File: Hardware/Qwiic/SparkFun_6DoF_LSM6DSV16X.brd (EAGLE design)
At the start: 25.4 x 25.4 mm, 78 parts, among them J1 QWIIC_RIGHT_ANGLE, J2 QWIIC_RIGHT_ANGLE, U2 LSM6DSV16X

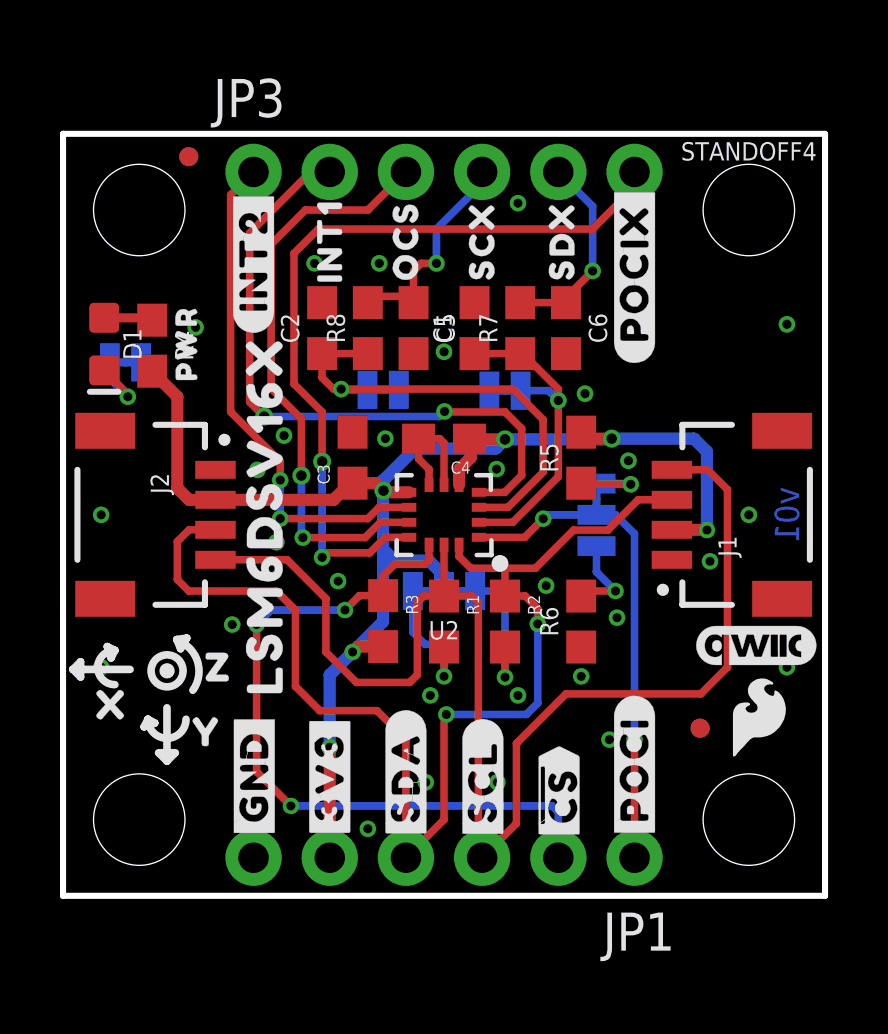
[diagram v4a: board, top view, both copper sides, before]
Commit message: Adds note about "Qvar sensing"
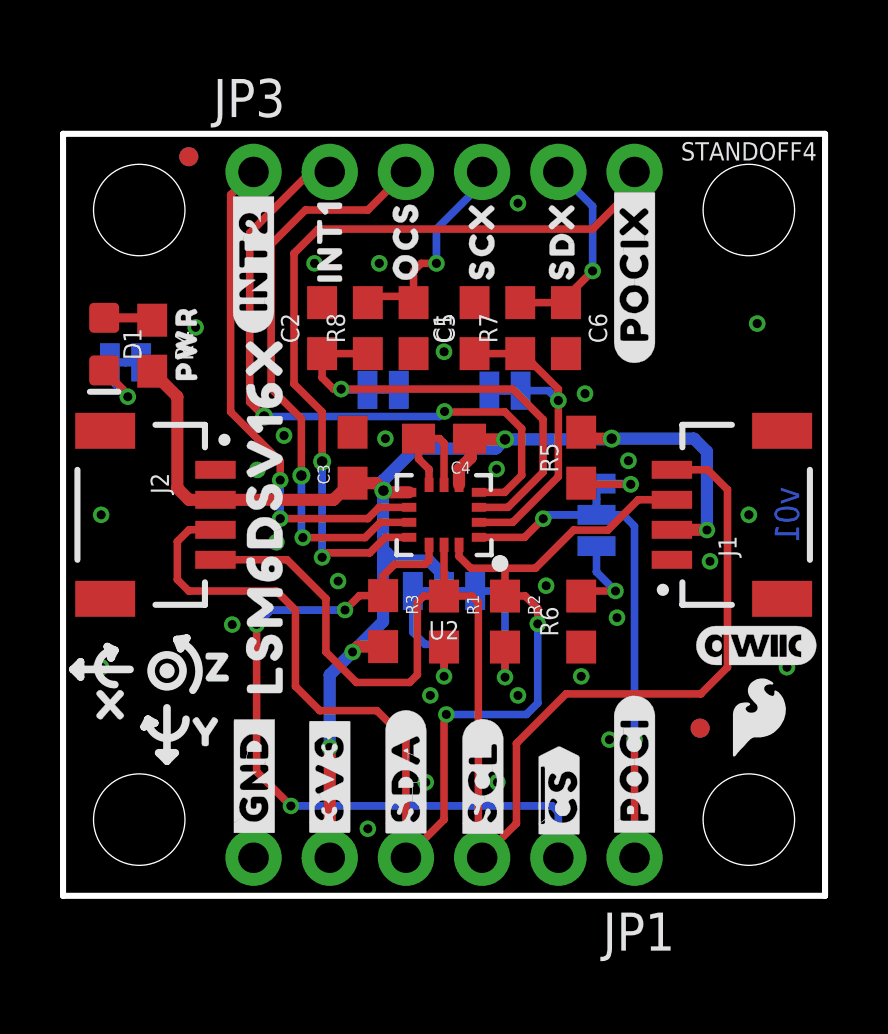
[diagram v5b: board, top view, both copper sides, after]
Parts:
- moved LOGO2 4.41 mm to (23.1, 19.1), turned to 270 degrees
- moved U$31 0.13 mm to (8.10, 12.7)
- moved U$46 0.13 mm to (6.48, 12.7)
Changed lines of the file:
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@@
 <setting verticaltext="up"/>
 </settings>
-<grid distance="0.05" unitdist="inch" unit="inch" style="dots" multiple="1" display="yes" altdistance="0.005" altunitdist="inch" altunit="inch"/>
+<grid distance="0.05" unitdist="inch" unit="inch" style="dots" multiple="1" display="yes" altdistance="0.001" altunitdist="inch" altunit="inch"/>
 <layers>
 <layer number="1" name="Top" color="4" fill="1" visible="yes" active="yes"/>
@@
 <layer number="27" name="tValues" color="7" fill="1" visible="no" active="yes"/>
 <layer number="28" name="bValues" color="7" fill="1" visible="no" active="yes"/>
-<layer number="29" name="tStop" color="7" fill="3" visible="yes" active="yes"/>
+<layer number="29" name="tStop" color="7" fill="3" visible="no" active="yes"/>
 <layer number="30" name="bStop" color="7" fill="6" visible="no" active="yes"/>
 <layer number="31" name="tCream" color="7" fill="4" visible="no" active="yes"/>
@@
 <attribute name="VALUE" x="13.716" y="16.383" size="0.4064" layer="27" font="vector" rot="R180"/>
 </element>
-<element name="LOGO2" library="SparkFun-Aesthetics" package="OSHW-LOGO-MINI" value="OSHW-LOGOMINI" x="23.7744" y="14.71295" smashed="yes" rot="MR0"/>
+<element name="LOGO2" library="SparkFun-Aesthetics" package="OSHW-LOGO-MINI" value="OSHW-LOGOMINI" x="23.13305" y="19.0754" smashed="yes" rot="MR270"/>
 <element name="STANDOFF1" library="SparkFun-Hardware" package="STAND-OFF-TIGHT" value="STAND-OFFTIGHT" x="2.54" y="22.86" smashed="yes"/>
 <element name="STANDOFF2" library="SparkFun-Hardware" package="STAND-OFF-TIGHT" value="STAND-OFFTIGHT" x="2.54" y="2.54" smashed="yes"/>
@@
 <element name="U$3" library="top" package="##CS##7" value="" x="16.5354" y="3.3528" smashed="yes" rot="R90"/>
 <element name="U$27" library="bot" package="##CS##8" value="" x="16.5354" y="3.3528" smashed="yes" rot="MR270"/>
-<element name="U$31" library="top" package="6DOF12" value="" x="7.9756" y="12.7" smashed="yes" rot="MR270"/>
+<element name="U$31" library="top" package="6DOF12" value="" x="8.1026" y="12.7" smashed="yes" rot="MR270"/>
 <element name="R5" library="SparkFun-Resistors" package="0603" value="10k" x="17.272" y="14.605" smashed="yes" rot="R90">
 <attribute name="NAME" x="16.51" y="14.605" size="0.6096" layer="25" font="vector" ratio="20" rot="R90" align="bottom-center"/>
@@
 <element name="U$42" library="top" package="#SDX#20" value="" x="14.732" y="15.367" smashed="yes" rot="MR0"/>
 <element name="U$43" library="top" package="#SCX#19" value="" x="10.668" y="15.367" smashed="yes" rot="MR0"/>
-<element name="U$46" library="top" package="LSM6DSV16X37" value="" x="6.35" y="12.7" smashed="yes" rot="MR270"/>
+<element name="U$46" library="top" package="LSM6DSV16X37" value="" x="6.477" y="12.7" smashed="yes" rot="MR270"/>
 <element name="U$47" library="top" package="LSM6DSV16X37" value="" x="6.731" y="12.7" smashed="yes" rot="R90"/>
 <element name="C5" library="SparkFun-Capacitors" package="0603" value="110pF" x="11.684" y="18.923" smashed="yes" rot="R270">
@@
 <via x="12.7" y="18.1356" extent="1-16" drill="0.3048"/>
 <via x="12.0904" y="3.7846" extent="1-16" drill="0.3"/>
-<via x="24.13" y="19.05" extent="1-16" drill="0.3048"/>
+<via x="23.1394" y="19.0754" extent="1-16" drill="0.3048"/>
 <via x="22.86" y="12.7" extent="1-16" drill="0.3048"/>
 <wire x1="12.2" y1="13.7" x2="12.2" y2="14.216" width="0.254" layer="1"/>
@@
 <wire x1="16.00481875" y1="12.57018125" x2="16.1346375" y2="12.7" width="0.254" layer="16"/>
 <wire x1="16.1346375" y1="12.7" x2="17.78" y2="12.7" width="0.254" layer="16"/>
-<wire x1="17.78" y1="12.7" x2="18.415" y2="12.7" width="0.254" layer="16"/>
+<wire x1="17.78" y1="12.7" x2="18.669" y2="12.7" width="0.254" layer="16"/>
 <via x="19.05" y="5.207" extent="1-16" drill="0.3"/>
 <contactref element="JP1" pad="1"/>
 <wire x1="19.05" y1="5.207" x2="19.05" y2="1.27" width="0.254" layer="1"/>
 <wire x1="19.0476" y1="5.2094" x2="19.05" y2="5.207" width="0.254" layer="16"/>
-<wire x1="18.415" y1="12.7" x2="19.0476" y2="12.0674" width="0.254" layer="16"/>
-<wire x1="19.0476" y1="12.0674" x2="19.0476" y2="5.2094" width="0.254" layer="16"/>
+<wire x1="18.669" y1="12.7" x2="19.0476" y2="12.3214" width="0.254" layer="16"/>
+<wire x1="19.0476" y1="12.3214" x2="19.0476" y2="5.2094" width="0.254" layer="16"/>
 <contactref element="U2" pad="P1"/>
 <wire x1="13.8625" y1="11.95" x2="15.3846375" y2="11.95" width="0.254" layer="1"/>

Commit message: Fixes airwire
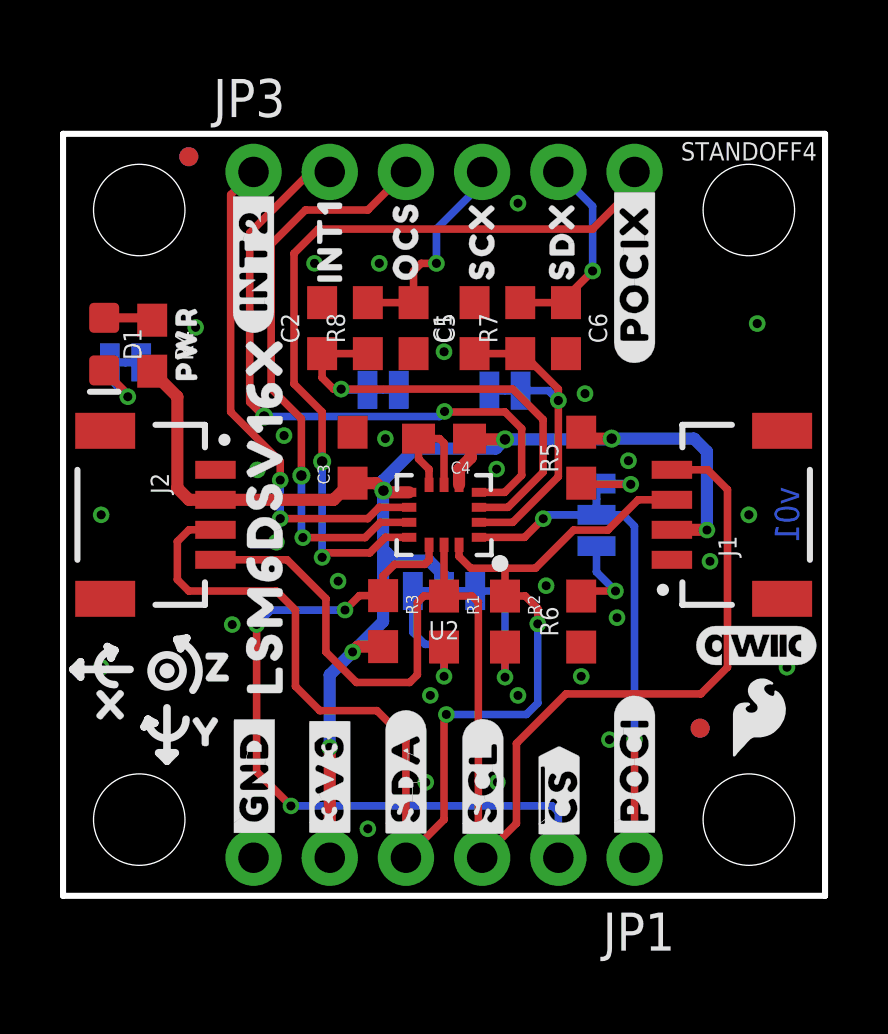
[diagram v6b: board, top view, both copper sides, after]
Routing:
- net SCX/AH2/QVAR2: track 7.85 -> 7.33 mm
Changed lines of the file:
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@@
 <setting verticaltext="up"/>
 </settings>
-<grid distance="0.05" unitdist="inch" unit="inch" style="dots" multiple="1" display="yes" altdistance="0.001" altunitdist="inch" altunit="inch"/>
+<grid distance="0.05" unitdist="inch" unit="inch" style="dots" multiple="1" display="yes" altdistance="0.005" altunitdist="inch" altunit="inch"/>
 <layers>
 <layer number="1" name="Top" color="4" fill="1" visible="yes" active="yes"/>
@@
 <wire x1="13.97" y1="23.749" x2="13.97" y2="24.13" width="0.254" layer="16"/>
 <wire x1="12.446" y1="22.225" x2="13.97" y2="23.749" width="0.254" layer="16"/>
-<wire x1="11.684" y1="19.773" x2="11.894" y2="19.983" width="0.1524" layer="1"/>
-<wire x1="10.16" y1="19.773" x2="10.37" y2="19.983" width="0.254" layer="1"/>
-<wire x1="10.243" y1="19.983" x2="11.894" y2="19.983" width="0.254" layer="1"/>
+<wire x1="11.684" y1="19.773" x2="11.8305" y2="19.9195" width="0.1524" layer="1"/>
 <wire x1="11.684" y1="19.773" x2="11.684" y2="20.828" width="0.254" layer="1"/>
 <wire x1="11.938" y1="21.082" x2="12.446" y2="21.082" width="0.254" layer="1"/>
@@
 <wire x1="12.446" y1="21.082" x2="12.446" y2="22.225" width="0.254" layer="16"/>
 <wire x1="11.684" y1="20.828" x2="11.938" y2="21.082" width="0.254" layer="1"/>
-<wire x1="10.243" y1="19.983" x2="10.37" y2="19.983" width="0" layer="19" extent="1-1"/>
+<wire x1="10.16" y1="19.773" x2="11.684" y2="19.773" width="0.254" layer="1"/>
 </signal>
 </signals>

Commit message: Adds jumpers for one of the DNP pads to select whether it's tied to 3v3 or GND
* Rolls to v10
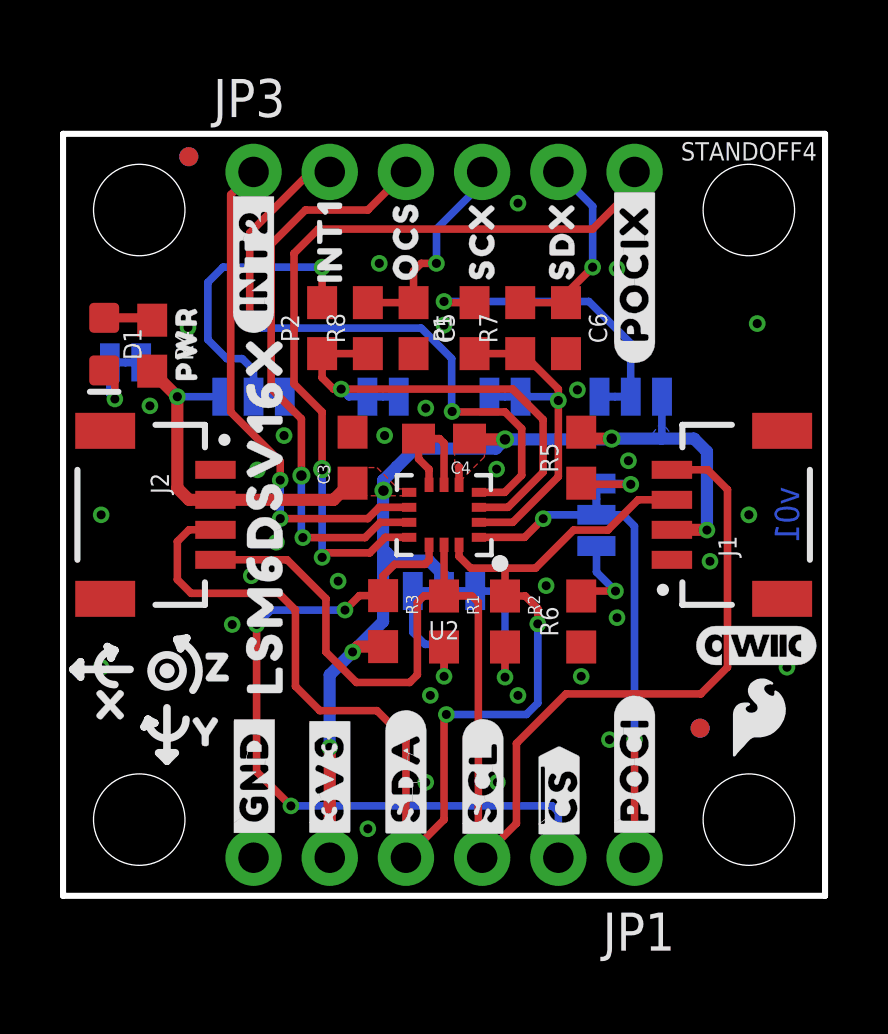
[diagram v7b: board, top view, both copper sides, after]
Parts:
- removed LOGO3: SFE_LOGO_NAME_FLAME.1_INCH, SparkFun-Aesthetics:SFE_LOGO_NAME_FLAME_.1
- added PAD1, PAD2: JUMPER-SMT_3_1-NC_TRACE_SILK, SparkFun-Jumpers:SMT-JUMPER_3_1-NC_TRACE_SILK
- added U$23: (no value), pot:#P1#4
- added U$30: (no value), pot:#P2#4
- added U$32: (no value), top:#1#729
- added U$41: (no value), pot:#1#4
- moved U$46 5.74 mm to (1.37, 10.1)
- moved U$31 5.51 mm to (3.07, 10.4)
- moved U$42 0.23 mm to (14.7, 15.1)
- moved SCX 0.23 mm to (10.7, 16.6)
- moved U$43 0.20 mm to (10.6, 15.2)
- moved SDX 0.20 mm to (14.7, 16.6)
- renumbered C1 to P1, C2 to P2
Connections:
- new net N$4: P2.2, PAD2.2
- new net N$8: P1.2, PAD1.2
- net 3.3V: now also PAD1.1, PAD2.1
- net GND: now also PAD1.3, PAD2.3; no longer P1.2, P2.2
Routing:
- net N$4: track 0.00 -> 9.94 mm, vias 0 -> 1
- net N$8: track 0.00 -> 9.61 mm, vias 0 -> 1
- net INT1: track 22.0 -> 21.3 mm
- net 3.3V: vias 6 -> 7
- net GND: vias 29 -> 32
- added copper zone on layer 1, net 3.3V
- added copper zone on layer 16, net 3.3V
